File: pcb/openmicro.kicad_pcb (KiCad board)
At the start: 4 copper layers, 95 x 95 mm, 101 parts, among them J1 ThumbPointer, J2 SWD_Header, J3 USB_C_Receptacle_2_0, SW1 RotaryEC11, SW10 KeySwitch, SW11 KeySwitch, SW12 KeySwitch, SW13 KeySwitch, SW14 KeySwitch, SW15 KeySwitch, SW2 ResetSwitch, SW3 KeySwitch, SW4 KeySwitch, SW5 KeySwitch, SW6 KeySwitch, SW7 KeySwitch, SW8 KeySwitch, SW9 KeySwitch, U1 USBLC6, U2 AP2112K_3V3, U3 STM32F072CBT6, Y1 Crystal8MHz

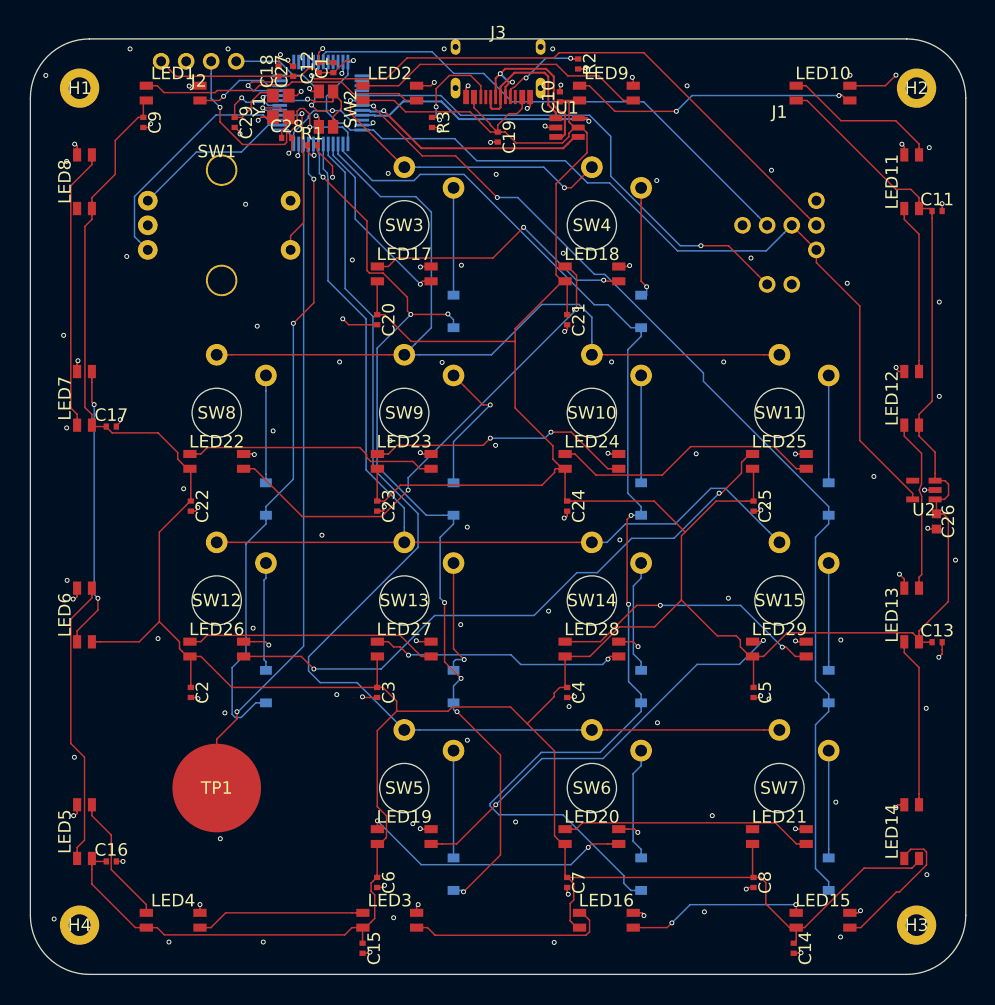
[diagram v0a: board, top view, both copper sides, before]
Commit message: Rework board design: GPIO re-derivation, passives library, 8-LED underglow
Hardware (CoHDL source + regenerated outputs):
- Re-derive the position-aware GPIO assignment; new pin map for matrix
  rows/cols, encoder, joystick, touch, and both LED chains
- Cut perimeter underglow from 16 to 8 SK6812MINI-E (2 per side)
- Drop the discrete reset switch and its footprint
- Move passives to the passive:: library with explicit voltage/dielectric
  specs; make every bypass cap a named instance, left unplaced for the
  RFC-027 auto-placer
- Regenerate netlist, layout, PCB, BOM/SMT, and gerbers (new layer-stack
  naming); add component datasheets under docs/; commit cohdl.lock

Firmware:
- Update pin tables to the new map; add a `proto` Cargo feature that
  keeps the pre-2026-07-28 prototype pin map and 16-LED ring buildable

Co-Authored-By: Claude Fable 5 <noreply@anthropic.com>
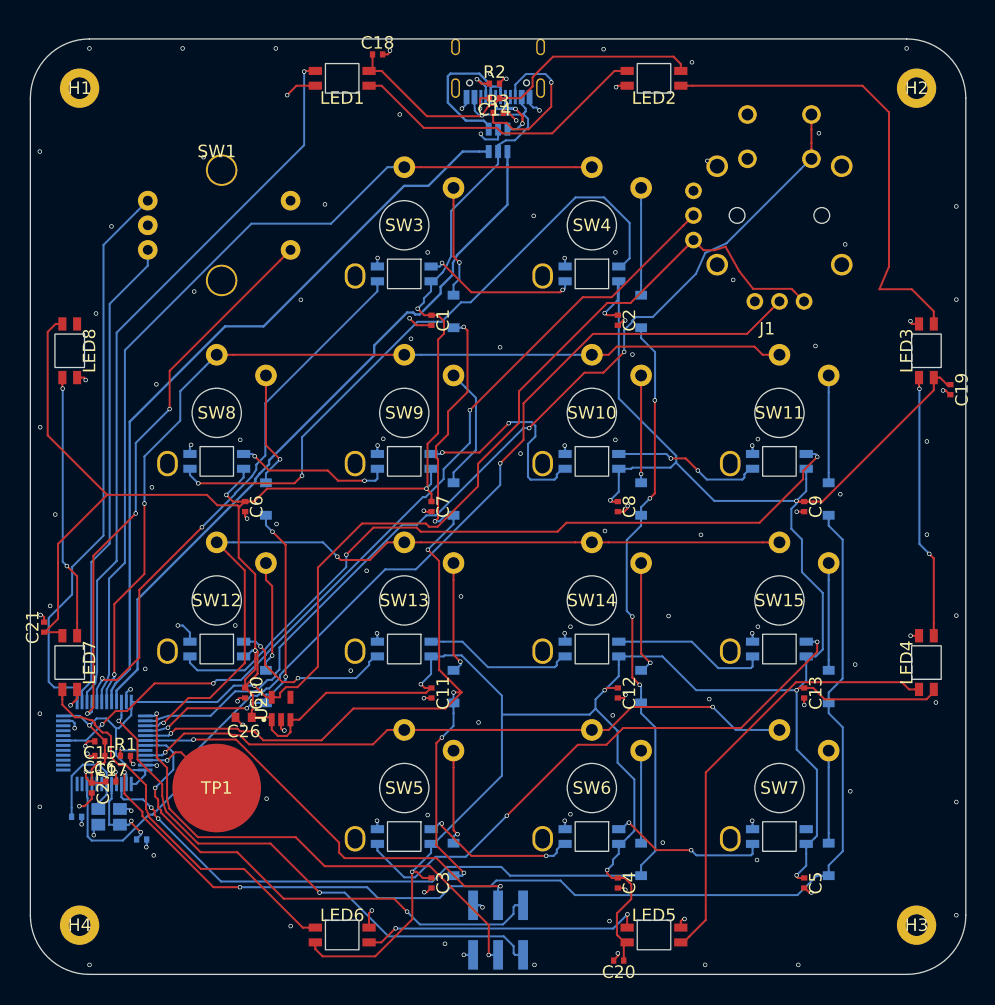
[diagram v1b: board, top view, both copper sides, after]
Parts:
- removed C22, C23, C24, C25: 100nF, std-CHIP_0402
- removed LED10, LED11, LED12, LED13, LED14, LED15, LED16, LED9: SK6812, openmicro-FP_LED_SK6812MINI_E
- removed SW2: ResetSwitch, openmicro-FP_SW_Reset
- C1, C10, C11, C12, C13, C14, C15, C16, C17, C18, C19, C2, C20, C21, C27, C3, C4, C5, C6, C7, C8, C9, R1, R2, R3: footprint std-CHIP_0402 -> passive-CHIP_0402
- C26: footprint std-CHIP_0603 -> passive-CHIP_0603
- C28, C29: footprint std-CHIP_0402 -> passive-CHIP_0402; moved to B.Cu
- J2: value SWD_Header -> Debug_2x3; footprint openmicro-FP_Header_1x4 -> openmicro-FP_Socket_2x3_254_SMD; moved to B.Cu
- J3, LED17, LED18, LED19, LED20, LED21, LED22, LED23, LED24, LED25, LED26, LED27, LED28, LED29, U1, Y1: moved to B.Cu
- moved J2 93.3 mm to (0.00, 43.0), turned to 0 degrees
- moved C14 91.5 mm to (-0.37, -41.5), turned to 180 degrees
- moved LED4 80.9 mm to (43.5, 15.8), turned to 90 degrees
- moved LED3 79.5 mm to (43.5, -15.8), turned to 90 degrees
- moved C9 77.6 mm to (31.1, -0.01)
- moved C27 75.6 mm to (-41.3, 28.6), turned to -90 degrees
- moved Y1 74.2 mm to (-39.5, 31.5), turned to 180 degrees
- moved C26 73.1 mm to (-25.8, 21.4), turned to 180 degrees
- moved C28 72.8 mm to (-36.2, 33.8)
- moved C29 72.3 mm to (-42.8, 31.5), turned to 0 degrees
- moved C11 70.9 mm to (-6.76, 18.9), turned to -90 degrees
- moved C12 70.4 mm to (12.2, 18.9), turned to -90 degrees
- moved C20 69.6 mm to (12.3, 46.1), turned to 180 degrees
- moved U2 68.9 mm to (-22.0, 20.5), turned to 90 degrees
- moved U3 68.6 mm to (-40.0, 24.0), turned to 90 degrees
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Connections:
- C1 pad 1: V3V3 -> VBUS
- C12 pad 1: V3V3 -> VBUS
- C15 pad 1: VBUS -> V3V3
- C16 pad 1: VBUS -> V3V3
- C17 pad 1: VBUS -> V3V3
- C18 pad 1: V3V3 -> VBUS
- J2 pad 1: SWDIO -> GND
- J2 pad 2: SWCLK -> GND
- J2 pad 3: GND -> SWCLK
- J2 pad 4: V3V3 -> UART_TX
- LED3 pad 2: UG_D11 -> UG_D3
- LED3 pad 4: UG_D10 -> UG_D2
- LED4 pad 2: UG_D12 -> UG_D4
- LED4 pad 4: UG_D11 -> UG_D3
- LED5 pad 2: UG_D13 -> UG_D5
- LED5 pad 4: UG_D12 -> UG_D4
- LED6 pad 2: UG_D14 -> UG_D6
- LED6 pad 4: UG_D13 -> UG_D5
- LED7 pad 2: UG_D15 -> UG_D7
- LED7 pad 4: UG_D14 -> UG_D6
- LED8 pad 4: UG_D15 -> UG_D7
- U1 pad 1: USBC_DP -> USBC_DM
- U1 pad 3: USBC_DM -> USBC_DP
- U1 pad 4: USB_DM -> USB_DP
- U1 pad 6: USB_DP -> USB_DM
- U3 pad 10: UG_D0 -> JOY_Y
- U3 pad 18: JOY_Y -> (no net)
- U3 pad 2: ENC_A -> COL3
- U3 pad 25: (no net) -> ENC_A
- U3 pad 26: (no net) -> ENC_B
- U3 pad 27: (no net) -> UG_D0
- U3 pad 28: (no net) -> ENC_SW
- U3 pad 29: JOY_SW -> LED_D0
- U3 pad 3: ENC_B -> COL2
- U3 pad 31: COL3 -> ROW1
- U3 pad 38: COL2 -> JOY_SW
- U3 pad 39: ROW1 -> ROW2
- U3 pad 4: ENC_SW -> (no net)
- U3 pad 40: LED_D0 -> COL0
- U3 pad 41: ROW3 -> COL1
- U3 pad 42: ROW2 -> UART_TX
- U3 pad 43: COL1 -> UART_RX
- U3 pad 45: COL0 -> ROW3
- U3 pad 7: NRST -> (no net)
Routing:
- net UG_D0: track 9.18 -> 74.3 mm
- net ROW0: track 31.0 -> 91.7 mm, vias 2 -> 0
- net TOUCH: track 69.1 -> 9.11 mm
- net VBUS: track 541.5 -> 486.4 mm, vias 0 -> 14
- net UART_RX: track 0.00 -> 53.0 mm, vias 0 -> 2
- net USB_DM: track 24.1 -> 77.0 mm, vias 1 -> 0
- net USB_DP: track 25.8 -> 73.3 mm, vias 1 -> 0
- net JOY_SW: track 51.5 -> 98.9 mm, vias 1 -> 2
- net UART_TX: track 0.00 -> 45.0 mm, vias 0 -> 2
- net ROW3: track 112.2 -> 68.3 mm, vias 0 -> 2
- net JOY_Y: track 61.6 -> 103.3 mm
- net ENC_A: track 16.6 -> 57.6 mm
- net ENC_SW: track 16.8 -> 57.2 mm, vias 1 -> 3
- net SWDIO: track 16.8 -> 55.8 mm
- net LED_D0: track 19.2 -> 55.5 mm, vias 1 -> 2
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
